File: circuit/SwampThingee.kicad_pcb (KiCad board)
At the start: 2 copper layers, 100 x 60 mm, 86 parts, among them J1 CONN_01X04, J2 HOLE, J3 HOLE, J4 HOLE, J5 HOLE, Q1 IRFS52N15DTRLP, Q2 BC547, SW1 RESET, SW10 4S, SW3 HEAD/AD, SW9 6S, U1 TPS560430, U2 LM1117-5.0, U3 MAX6457, U4 LM1117-3.3, U5 TPA3220, U6 CSR_DebugSmall, U7 CSR8645_MODULE

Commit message: swamp thingee first draft done
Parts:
- moved SW10 2.54 mm to (76.8, 72.4)
- moved SW9 2.54 mm to (76.8, 69.8)
- moved R1 0.64 mm to (85.1, 81.3)
- moved R6 0.64 mm to (85.1, 83.2)
- moved R8 0.64 mm to (85.1, 77.5)
- moved R9 0.64 mm to (85.1, 79.4)
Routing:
- net +BATT: track 148.7 -> 194.4 mm
- net GND: track 0.00 -> 39.4 mm, vias 0 -> 60
- net /GAIN_SLV: track 0.00 -> 39.0 mm
- net OTW_CLIP: track 0.00 -> 37.0 mm
- net -BATT: track 0.00 -> 33.5 mm
- net FAULT: track 0.00 -> 20.7 mm
- net Net-(C25-Pad1): track 0.00 -> 18.5 mm
- net /MAX_VDIV: track 0.00 -> 17.9 mm
- net Net-(C15-Pad2): track 0.00 -> 17.6 mm
- net Net-(C36-Pad2): track 0.00 -> 16.0 mm
- net /SW_GATE: track 0.00 -> 15.5 mm
- net Net-(C5-Pad1): track 0.00 -> 14.1 mm
- net Net-(R8-Pad1): track 0.00 -> 12.4 mm
- net Net-(R9-Pad1): track 0.00 -> 12.0 mm
- net +7.5V: track 24.2 -> 33.2 mm
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- added copper zone on B.Cu, net GND
- added copper zone on F.Cu, net GND

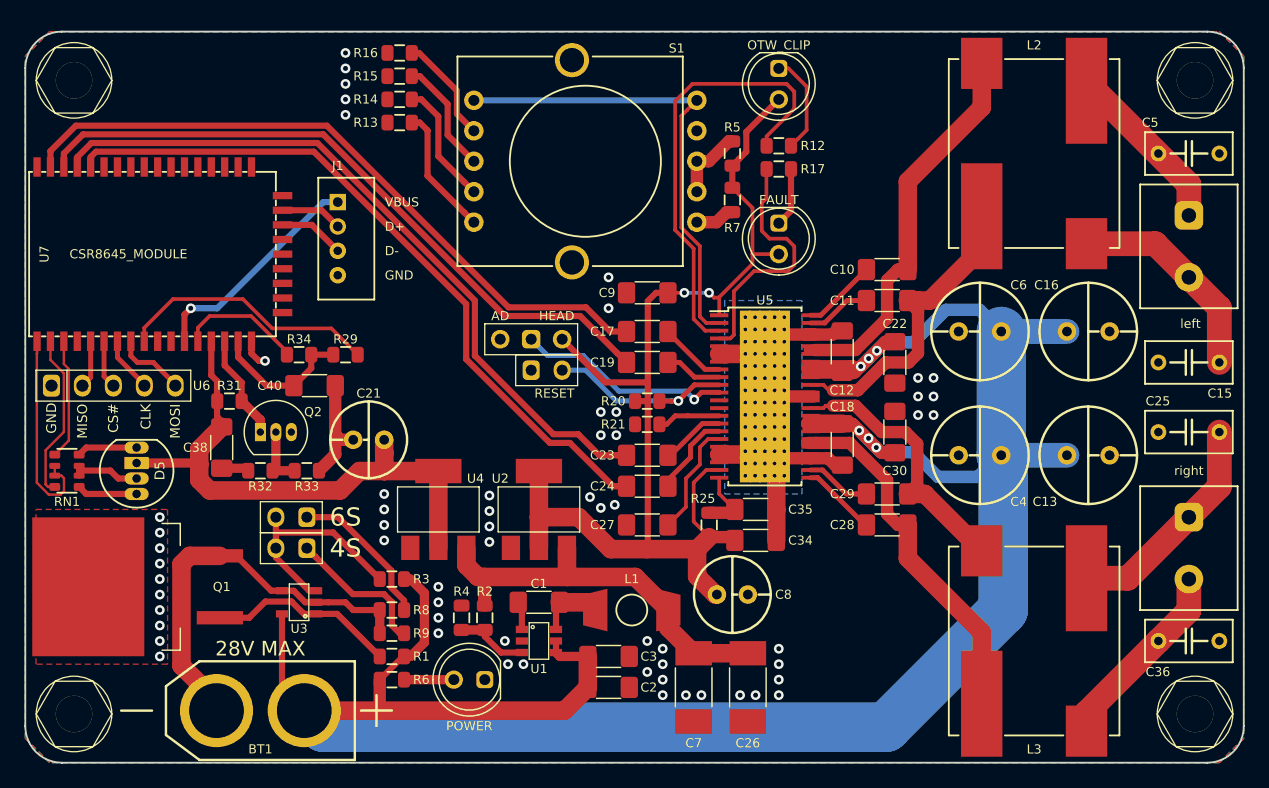
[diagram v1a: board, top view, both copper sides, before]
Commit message: sent swamp thingee to the fab added the face of swamp thing
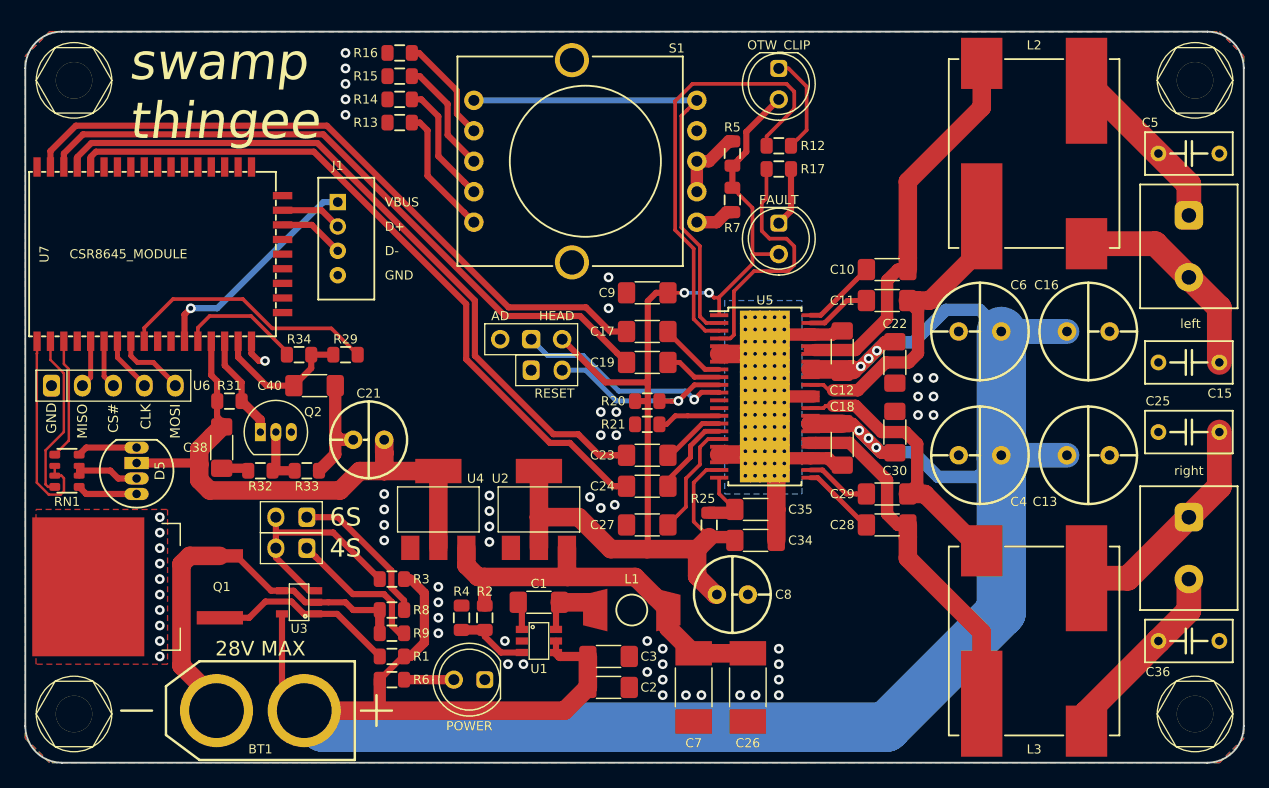
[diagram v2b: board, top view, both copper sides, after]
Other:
- board text added: "2019.04.07"
- board text added: "https://github.com/nodep/NovaBox"
- board text added: "swamp thingee"
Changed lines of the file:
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@@
   (general
     (thickness 1.6)
-    (drawings 17)
-    (tracks 597)
+    (drawings 20)
+    (tracks 596)
     (zones 0)
     (modules 86)
@@
   )
   (setup
-    (last_trace_width 2.032)
+    (last_trace_width 0.2032)
     (user_trace_width 0.254)
     (user_trace_width 0.3048)
@@
     (add_net VBUS)
   )
+  (module NovaBox:CSR_DebugSmall (layer F.Cu)
+    (at 62.23 59.055)
+    (fp_text reference U6 (at 7.239 0 180) (layer F.SilkS)
+      (effects (font (size 0.762 0.762) (thickness 0.127)))
+    )
+    (fp_text value CSR_DebugSmall (at -1 0 -270) (layer F.Fab) hide
+      (effects (font (size 0.127 0.127) (thickness 0.0127)))
+    )
+    (fp_text user GND (at -5.08 2.667 90) (layer F.SilkS)
+      (effects (font (size 0.8128 0.8128) (thickness 0.1524)))
+    )
+    (fp_text user MISO (at -2.54 2.921 90) (layer F.SilkS)
+      (effects (font (size 0.8128 0.8128) (thickness 0.1524)))
+    )
+    (fp_text user CS# (at 0 2.667 90) (layer F.SilkS)
+      (effects (font (size 0.8128 0.8128) (thickness 0.1524)))
+    )
+    (fp_text user CLK (at 2.667 2.54 90) (layer F.SilkS)
+      (effects (font (size 0.8128 0.8128) (thickness 0.1524)))
+    )
+    (fp_text user MOSI (at 5.08 2.921 90) (layer F.SilkS)
+      (effects (font (size 0.8128 0.8128) (thickness 0.1524)))
+    )
+    (fp_line (start -6.35 -1.27) (end -6.35 1.27) (layer F.SilkS) (width 0.1))
+    (fp_line (start 6.35 -1.27) (end -6.35 -1.27) (layer F.SilkS) (width 0.1))
+    (fp_line (start 6.35 1.27) (end 6.35 -1.27) (layer F.SilkS) (width 0.1))
+    (fp_line (start -6.35 1.27) (end 6.35 1.27) (layer F.SilkS) (width 0.1))
+    (fp_line (start -3.81 -1.27) (end -3.81 1.27) (layer F.SilkS) (width 0.1))
+    (pad 1 thru_hole oval (at 5.08 0) (size 1.4 1.8) (drill 0.9) (layers *.Cu *.Mask)
+      (net 66 /MOSI))
+    (pad 2 thru_hole oval (at 2.54 0) (size 1.4 1.8) (drill 0.9) (layers *.Cu *.Mask)
+      (net 65 /CLK))
+    (pad 3 thru_hole oval (at 0 0) (size 1.4 1.8) (drill 0.9) (layers *.Cu *.Mask)
+      (net 64 /CS#))
+    (pad 4 thru_hole oval (at -2.54 0) (size 1.4 1.8) (drill 0.9) (layers *.Cu *.Mask)
+      (net 63 /MISO))
+    (pad 5 thru_hole roundrect (at -5.08 0) (size 1.4 1.8) (drill 0.9) (layers *.Cu *.Mask) (roundrect_rratio 0.25)
+      (net 3 GND))
+    (model Pin_Headers.3dshapes/Pin_Header_Straight_1x05.wrl
+      (at (xyz 0 0 0))
+      (scale (xyz 1 1 1))
+      (rotate (xyz 0 0 0))
+    )
+  )
   (module NovaBox:C_1812 (layer F.Cu)
     (at 114.3 83.82 90)
@@
     (fp_line (start -3.1 0) (end -1.55 2.684) (layer F.SilkS) (width 0.1))
     (pad 1 thru_hole circle (at 0 0) (size 3 3) (drill 3) (layers *.Cu *.Mask))
-  )
-  (module NovaBox:CSR_DebugSmall (layer F.Cu)
-    (at 62.23 59.055)
-    (fp_text reference U6 (at 7.239 0 180) (layer F.SilkS)
-      (effects (font (size 0.762 0.762) (thickness 0.127)))
-    )
-    (fp_text value CSR_DebugSmall (at -1 0 -270) (layer F.Fab) hide
-      (effects (font (size 0.127 0.127) (thickness 0.0127)))
-    )
-    (fp_text user GND (at -5.08 2.667 90) (layer F.SilkS)
-      (effects (font (size 0.8128 0.8128) (thickness 0.1524)))
-    )
-    (fp_text user MISO (at -2.54 2.921 90) (layer F.SilkS)
-      (effects (font (size 0.8128 0.8128) (thickness 0.1524)))
-    )
-    (fp_text user CS# (at 0 2.667 90) (layer F.SilkS)
-      (effects (font (size 0.8128 0.8128) (thickness 0.1524)))
-    )
-    (fp_text user CLK (at 2.667 2.54 90) (layer F.SilkS)
-      (effects (font (size 0.8128 0.8128) (thickness 0.1524)))
-    )
-    (fp_text user MOSI (at 5.08 2.921 90) (layer F.SilkS)
-      (effects (font (size 0.8128 0.8128) (thickness 0.1524)))
-    )
-    (fp_line (start -6.35 -1.27) (end -6.35 1.27) (layer F.SilkS) (width 0.1))
-    (fp_line (start 6.35 -1.27) (end -6.35 -1.27) (layer F.SilkS) (width 0.1))
-    (fp_line (start 6.35 1.27) (end 6.35 -1.27) (layer F.SilkS) (width 0.1))
-    (fp_line (start -6.35 1.27) (end 6.35 1.27) (layer F.SilkS) (width 0.1))
-    (fp_line (start -3.81 -1.27) (end -3.81 1.27) (layer F.SilkS) (width 0.1))
-    (pad 1 thru_hole oval (at 5.08 0) (size 1.4 1.8) (drill 1) (layers *.Cu *.Mask)
-      (net 66 /MOSI))
-    (pad 2 thru_hole oval (at 2.54 0) (size 1.4 1.8) (drill 1) (layers *.Cu *.Mask)
-      (net 65 /CLK))
-    (pad 3 thru_hole oval (at 0 0) (size 1.4 1.8) (drill 1) (layers *.Cu *.Mask)
-      (net 64 /CS#))
-    (pad 4 thru_hole oval (at -2.54 0) (size 1.4 1.8) (drill 1) (layers *.Cu *.Mask)
-      (net 63 /MISO))
-    (pad 5 thru_hole roundrect (at -5.08 0) (size 1.4 1.8) (drill 1) (layers *.Cu *.Mask) (roundrect_rratio 0.25)
-      (net 3 GND))
-    (model Pin_Headers.3dshapes/Pin_Header_Straight_1x05.wrl
-      (at (xyz 0 0 0))
-      (scale (xyz 1 1 1))
-      (rotate (xyz 0 0 0))
-    )
   )
   (module NovaBox:R_0805 (layer F.Cu)
@@
     )
   )
+  (gr_text https://github.com/nodep/NovaBox (at 121.285 71.755) (layer B.SilkS)
+    (effects (font (size 2 2) (thickness 0.3)) (justify mirror))
+  )
+  (gr_text 2019.04.07 (at 136.525 33.02) (layer B.SilkS)
+    (effects (font (size 2 2) (thickness 0.3)) (justify mirror))
+  )
+  (gr_text "swamp\nthingee" (at 63.5 34.925) (layer F.SilkS)
+    (effects (font (size 3 3) (thickness 0.5) italic) (justify left))
+  )
   (gr_line (start 62.865 85.725) (end 65.405 85.725) (layer F.SilkS) (width 0.2))
   (gr_line (start 83.82 84.455) (end 83.82 86.995) (layer F.SilkS) (width 0.2))
@@
   (segment (start 135.1 54.61) (end 137.795 54.61) (width 2.032) (layer B.Cu) (net 2))
   (segment (start 137.795 54.61) (end 140.49 54.61) (width 2.032) (layer B.Cu) (net 2))
+  (segment (start 78.105 85.725) (end 77.895 85.725) (width 4.064) (layer B.Cu) (net 2))
+  (segment (start 79.470201 87.090201) (end 78.105 85.725) (width 4.064) (layer B.Cu) (net 2))
+  (segment (start 125.634799 87.090201) (end 79.470201 87.090201) (width 4.064) (layer B.Cu) (net 2))
   (segment (start 135.1 54.61) (end 135.1 64.77) (width 4.064) (layer B.Cu) (net 2))
-  (segment (start 135.255 64.925) (end 135.1 64.77) (width 4.064) (layer B.Cu) (net 2))
-  (segment (start 135.255 77.47) (end 135.255 64.925) (width 4.064) (layer B.Cu) (net 2))
-  (segment (start 125.634799 87.090201) (end 135.255 77.47) (width 4.064) (layer B.Cu) (net 2))
-  (segment (start 79.470201 87.090201) (end 125.634799 87.090201) (width 4.064) (layer B.Cu) (net 2))
-  (segment (start 77.895 85.725) (end 78.105 85.725) (width 4.064) (layer B.Cu) (net 2))
-  (segment (start 78.105 85.725) (end 79.470201 87.090201) (width 4.064) (layer B.Cu) (net 2))
+  (segment (start 135.1 77.625) (end 125.634799 87.090201) (width 4.064) (layer B.Cu) (net 2))
+  (segment (start 135.1 64.77) (end 135.1 77.625) (width 4.064) (layer B.Cu) (net 2))
   (segment (start 116.497 65.31) (end 116.497 65.444) (width 1.016) (layer F.Cu) (net 3))
   (segment (start 116.7922 65.0148) (end 116.497 65.31) (width 1.016) (layer F.Cu) (net 3))
